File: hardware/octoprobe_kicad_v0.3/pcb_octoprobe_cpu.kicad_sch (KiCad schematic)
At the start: 42 parts, among them J201 BOOT Button, Q201 NMOS, Q202 NMOS, SW201 RESET, U201 RP2040, U202 AMS1117-3.3, U203 W25Q128JVS, Y201 Crystal_GND24_Small

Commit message: PCB: Octobus
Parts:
- BP203: value GPIO12 -> GPIO11
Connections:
- net RELAIS_5: now also U201.7 (GPIO5); no longer U201.11 (GPIO8)
- net RELAIS_6: now reaches U201.8 (GPIO6)
- net RELAIS_7: now reaches U201.9 (GPIO7)
- no-connect marks 19 -> 17
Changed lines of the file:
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@@
 	)
 	(no_connect
-		(at 44.45 57.15)
-	)
-	(no_connect
 		(at 44.45 87.63)
 	)
@@
 	)
 	(no_connect
+		(at 44.45 64.77)
+	)
+	(no_connect
 		(at 115.57 52.07)
 	)
@@
 	)
 	(no_connect
-		(at 44.45 54.61)
-	)
-	(no_connect
 		(at 44.45 100.33)
 	)
@@
 	)
 	(no_connect
-		(at 44.45 59.69)
-	)
-	(no_connect
 		(at 44.45 97.79)
 	)
@@
 		)
 	)
+	(global_label "RELAIS_7"
+		(shape output)
+		(at 44.45 59.69 180)
+		(fields_autoplaced yes)
+		(effects
+			(font
+				(size 1.27 1.27)
+			)
+			(justify right)
+		)
+		(property "Intersheetrefs" "${INTERSHEET_REFS}"
+			(at 32.8426 59.69 0)
+			(effects
+				(font
+					(size 1.27 1.27)
+				)
+				(justify right)
+				(hide yes)
+			)
+		)
+	)
+	(global_label "RELAIS_6"
+		(shape output)
+		(at 44.45 57.15 180)
+		(fields_autoplaced yes)
+		(effects
+			(font
+				(size 1.27 1.27)
+			)
+			(justify right)
+		)
+		(property "Intersheetrefs" "${INTERSHEET_REFS}"
+			(at 32.8426 57.15 0)
+			(effects
+				(font
+					(size 1.27 1.27)
+				)
+				(justify right)
+				(hide yes)
+			)
+		)
+	)
 	(global_label "RP2-USB-DP"
 		(shape input)
@@
 	(global_label "RELAIS_5"
 		(shape output)
-		(at 44.45 64.77 180)
+		(at 44.45 54.61 180)
 		(fields_autoplaced yes)
 		(effects
@@
 		)
 		(property "Intersheetrefs" "${INTERSHEET_REFS}"
-			(at 32.8426 64.77 0)
+			(at 32.8426 54.61 0)
 			(effects
 				(font
@@
 			)
 		)
-		(property "Value" "GPIO12"
+		(property "Value" "GPIO11"
 			(at 28.448 72.39 0)
 			(effects

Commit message: PCB: Oscillator
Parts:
- removed C201, C202: 30p, Capacitor_SMD:C_0402_1005Metric, symbol 00_project_library:C
- removed R201: 1k, Resistor_SMD:R_0402_1005Metric, symbol Device:R
- removed Y201: Crystal_GND24_Small, 00_project_library:Crystal_SMD_3225-4Pin_3.2x2.5mm, symbol 00_project_library:Crystal_GND24_Small
- added X201: Oscillator-12MHz, Oscillator:Oscillator_SMD_ECS_2520MV-xxx-xx-4Pin_2.5x2.0mm, symbol 00_project_library:Oscillator-12MHz
- R202: footprint Resistor_SMD:R_0603_1608Metric -> Resistor_SMD:R_0805_2012Metric
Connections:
- net +3V3: now also X201.4 (VDD)
- net GND: now also X201.2 (GND)
- net XIN: now also X201.3 (OUT)
- net XOUT: no longer names the net of U201.21 (XOUT)
- no-connect marks 17 -> 19
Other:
- note added: "JLC alternatives | jlc | USD/Stock | Package | Comments | | - | - | - | - | | C2901596 | 0.37/1k | SMD2520-4P | 1th | | C437139 | 0.29/188 | SMD2520-4P | 2nd | | C2831468 | 0.37/1k | SMD2520-4P | 2nd | | C387449 | 0.49/3k | SMD2520-4P | 2nd | | C409301 | 0.55/2k | SMD2520-4P | 2nd |"
- note added: "Oscillator"
- note removed: "C1, C2 = 2*CL - 2*Cs CL = 20pF, Cs can be ~5pF"
- note removed: "Crystal"

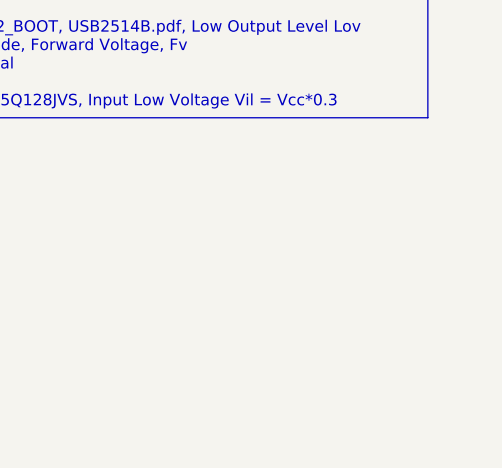
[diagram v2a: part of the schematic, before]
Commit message: PCB: Add "Open Hardware"
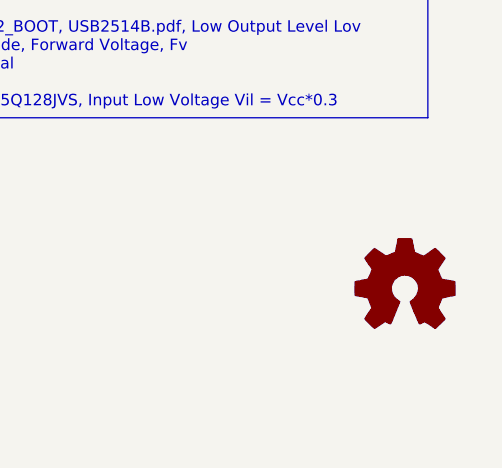
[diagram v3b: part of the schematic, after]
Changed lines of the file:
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@@
+	)
+	(symbol
+		(lib_id "Graphic:Logo_Open_Hardware_Small")
+		(at 275.59 175.26 0)
+		(unit 1)
+		(exclude_from_sim yes)
+		(in_bom no)
+		(on_board no)
+		(dnp no)
+		(fields_autoplaced yes)
+		(property "Reference" "#SYM201"
+			(at 275.59 168.275 0)
+			(effects
+				(font
+					(size 1.27 1.27)
+				)
+				(hide yes)
+			)
+		)
+		(property "Value" "Logo_Open_Hardware_Small"
+			(at 275.59 180.975 0)
+			(effects
+				(font
+					(size 1.27 1.27)
+				)
+				(hide yes)
+			)
+		)
+		(property "Footprint" ""
+			(at 275.59 175.26 0)
+			(effects
+				(font
+					(size 1.27 1.27)
+				)
+				(hide yes)
+			)
+		)
+		(property "Datasheet" "~"
+			(at 275.59 175.26 0)
+			(effects
+				(font
+					(size 1.27 1.27)
+				)
+				(hide yes)
+			)
+		)
+		(property "Description" "Open Hardware logo, small"
+			(at 275.59 175.26 0)
+			(effects
+				(font
+					(size 1.27 1.27)
+				)
+				(hide yes)
+			)
+		)
+		(instances
+			(project "pcb_octoprobe"
+				(path "/35c47459-45a7-4753-acae-c8b47e7575e1/24d7d496-8920-4421-a637-0c9bf263a085"
+					(reference "#SYM201")
+					(unit 1)
+				)
+			)
+		)
 	)
 	(symbol

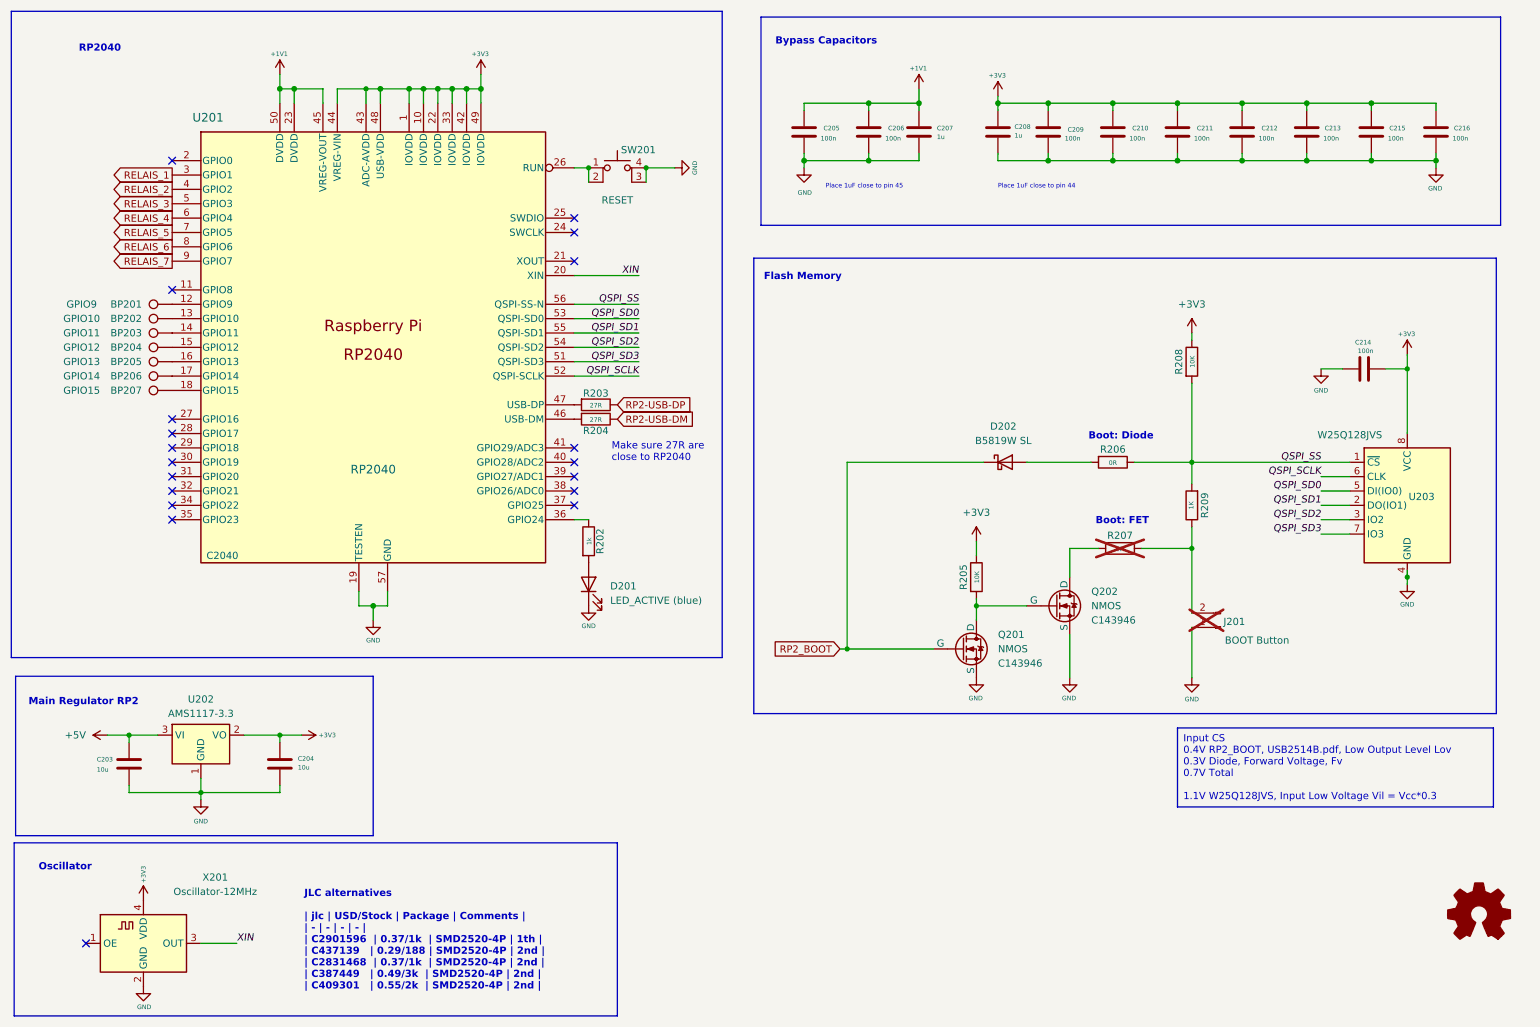
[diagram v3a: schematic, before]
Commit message: PCB: Production files ready
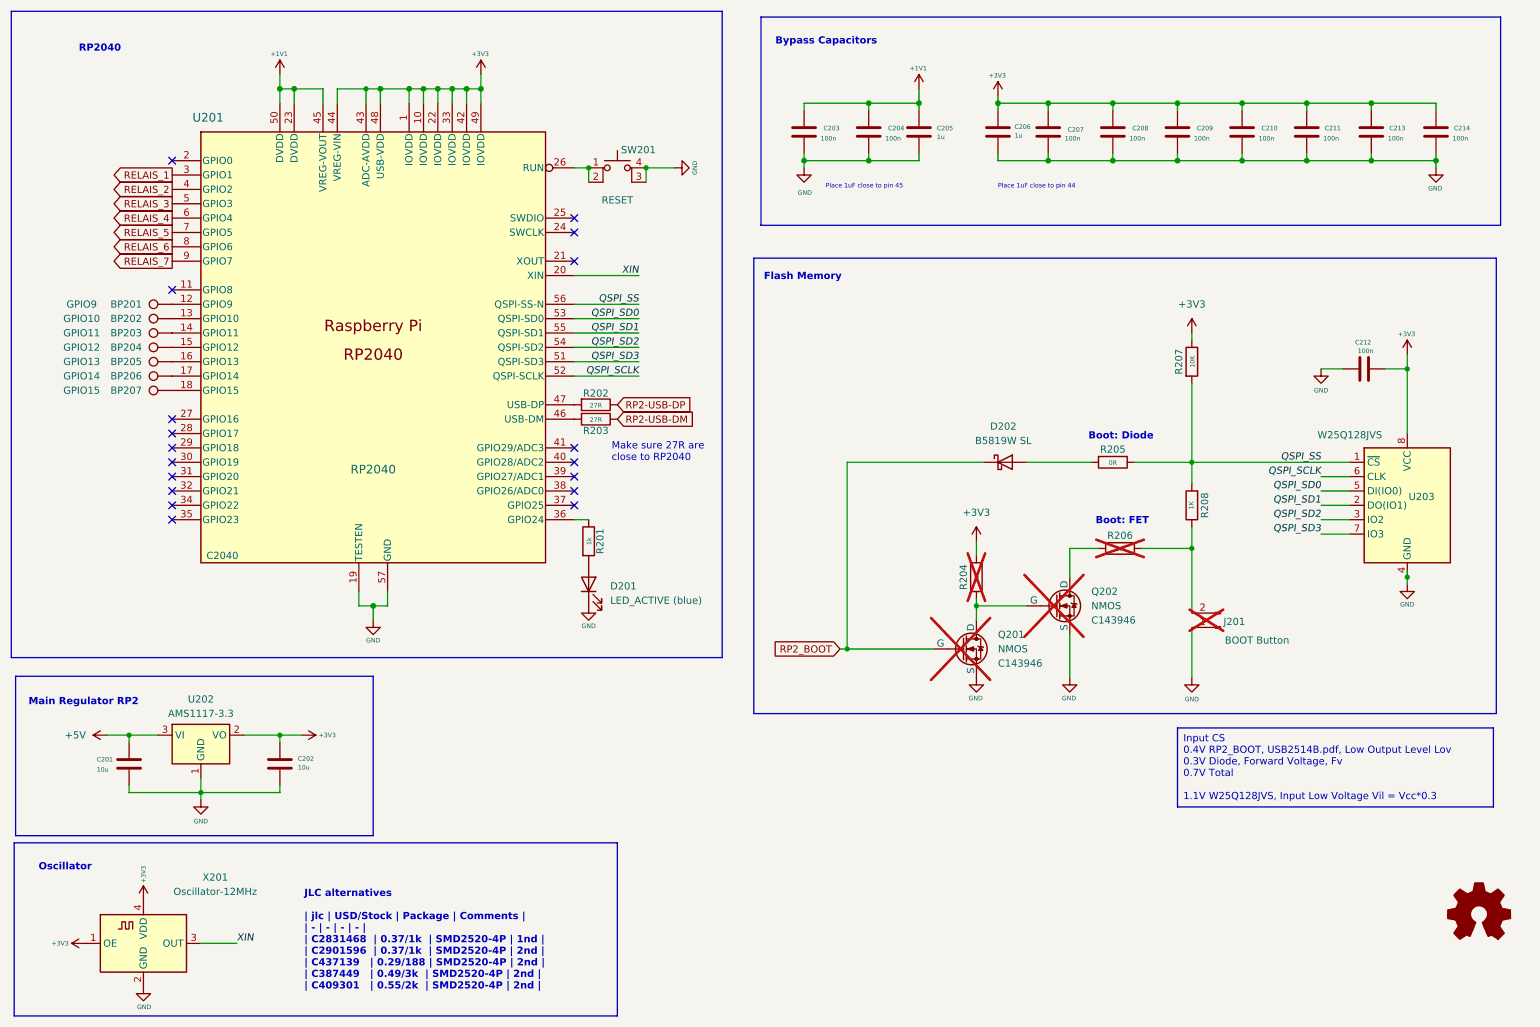
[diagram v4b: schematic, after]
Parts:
- D201: footprint 00_project_library:LED_0603_1608Metric -> LED_SMD:LED_0805_2012Metric
- Q201, Q202: now not fitted
- R204: renamed from R205; footprint Resistor_SMD:R_0402_1005Metric -> Resistor_SMD:R_0805_2012Metric; now not fitted
- X201: JLC C2901596 -> C2831468
- renumbered C203 to C201, C204 to C202, C205 to C203, C206 to C204, C207 to C205, C208 to C206, C209 to C207, C210 to C208, C211 to C209, C212 to C210, C213 to C211, C214 to C212, C215 to C213, C216 to C214, R202 to R201, R203 to R202, R204 to R203, R206 to R205, R207 to R206, R208 to R207, R209 to R208
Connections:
- net +3V3: now also X201.1 (OE)
- no-connect marks 19 -> 18
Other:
- note added: "JLC alternatives | jlc | USD/Stock | Package | Comments | | - | - | - | - | | C2831468 | 0.37/1k | SMD2520-4P | 1nd | | C2901596 | 0.37/1k | SMD2520-4P | 2nd | | C437139 | 0.29/188 | SMD2520-4P | 2nd | | C387449 | 0.49/3k | SMD2520-4P | 2nd | | C409301 | 0.55/2k | SMD2520-4P | 2nd |"
- note removed: "JLC alternatives | jlc | USD/Stock | Package | Comments | | - | - | - | - | | C2901596 | 0.37/1k | SMD2520-4P | 1th | | C437139 | 0.29/188 | SMD2520-4P | 2nd | | C2831468 | 0.37/1k | SMD2520-4P | 2nd | | C387449 | 0.49/3k | SMD2520-4P | 2nd | | C409301 | 0.55/2k | SMD2520-4P | 2nd |"
